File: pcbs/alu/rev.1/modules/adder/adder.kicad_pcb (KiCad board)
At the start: 2 copper layers, 76.2 x 80.6 mm, 513 parts, among them J1 Conn_01x01, J10 Conn_01x01, J11 Conn_01x01, J12 Conn_01x01, J13 Conn_01x01, J14 Conn_01x01, J15 Conn_01x01, J16 Conn_01x01, J17 Conn_01x01, J18 Conn_01x01, J19 Conn_01x01, J2 Conn_01x01, J20 Conn_01x01, J21 Conn_01x01, J22 Conn_01x01, J23 Conn_01x01, J24 Conn_01x01, J25 Conn_01x01, J26 Conn_01x01, J27 Conn_01x01, J28 Conn_01x01, J29 Conn_01x01, J3 Conn_01x01, J30 Conn_01x01, J31 Conn_01x01, J32 Conn_01x01, J33 Conn_01x01, J34 Conn_01x01, J35 Conn_01x01, J36 Conn_01x01, J4 Conn_01x01, J5 Conn_01x01, J6 Conn_01x01, J7 Conn_01x01, J8 Conn_01x01, J9 Conn_01x01, Q1 BSS8402DW, Q10 BSS8402DW, Q100 BSS8402DW, Q101 BSS8402DW, Q102 BSS8402DW, Q103 BSS8402DW, Q104 BSS8402DW, Q105 BSS8402DW, Q106 BSS8402DW, Q107 BSS8402DW, Q108 BSS8402DW, Q109 BSS8402DW, Q11 BSS8402DW, Q110 BSS8402DW, Q111 BSS8402DW, Q112 BSS8402DW, Q113 BSS8402DW, Q114 BSS8402DW, Q115 BSS8402DW, Q116 BSS8402DW, Q117 BSS8402DW, Q118 BSS8402DW, Q119 BSS8402DW, Q12 BSS8402DW, Q120 BSS8402DW, Q121 BSS8402DW, Q122 BSS8402DW, Q123 BSS8402DW, Q124 BSS8402DW, Q125 BSS8402DW, Q126 BSS8402DW, Q127 BSS8402DW, Q128 BSS8402DW, Q129 BSS8402DW, Q13 BSS8402DW, Q130 BSS8402DW, Q131 BSS8402DW, Q132 BSS8402DW, Q133 BSS8402DW, Q134 BSS8402DW, Q135 BSS8402DW, Q136 BSS8402DW, Q137 BSS8402DW, Q138 BSS8402DW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

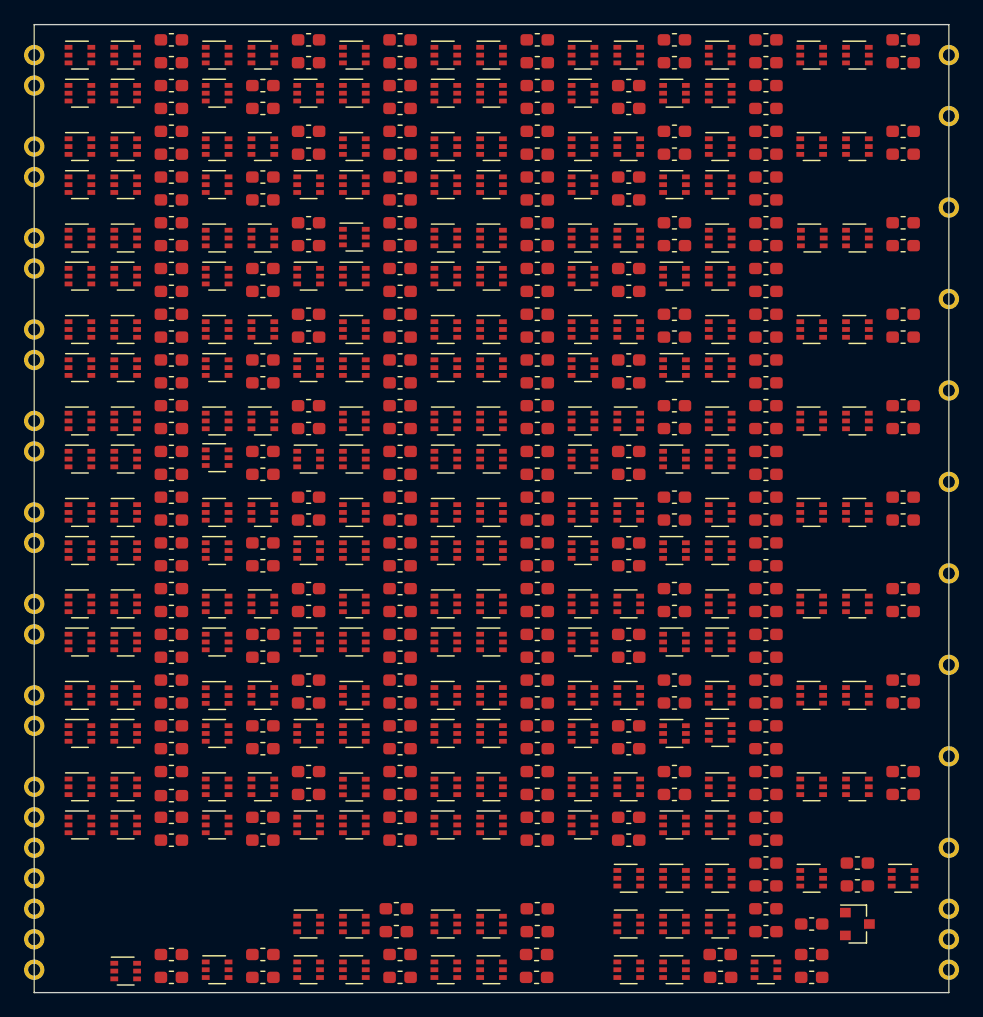
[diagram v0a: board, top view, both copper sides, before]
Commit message: completed adder module for alu
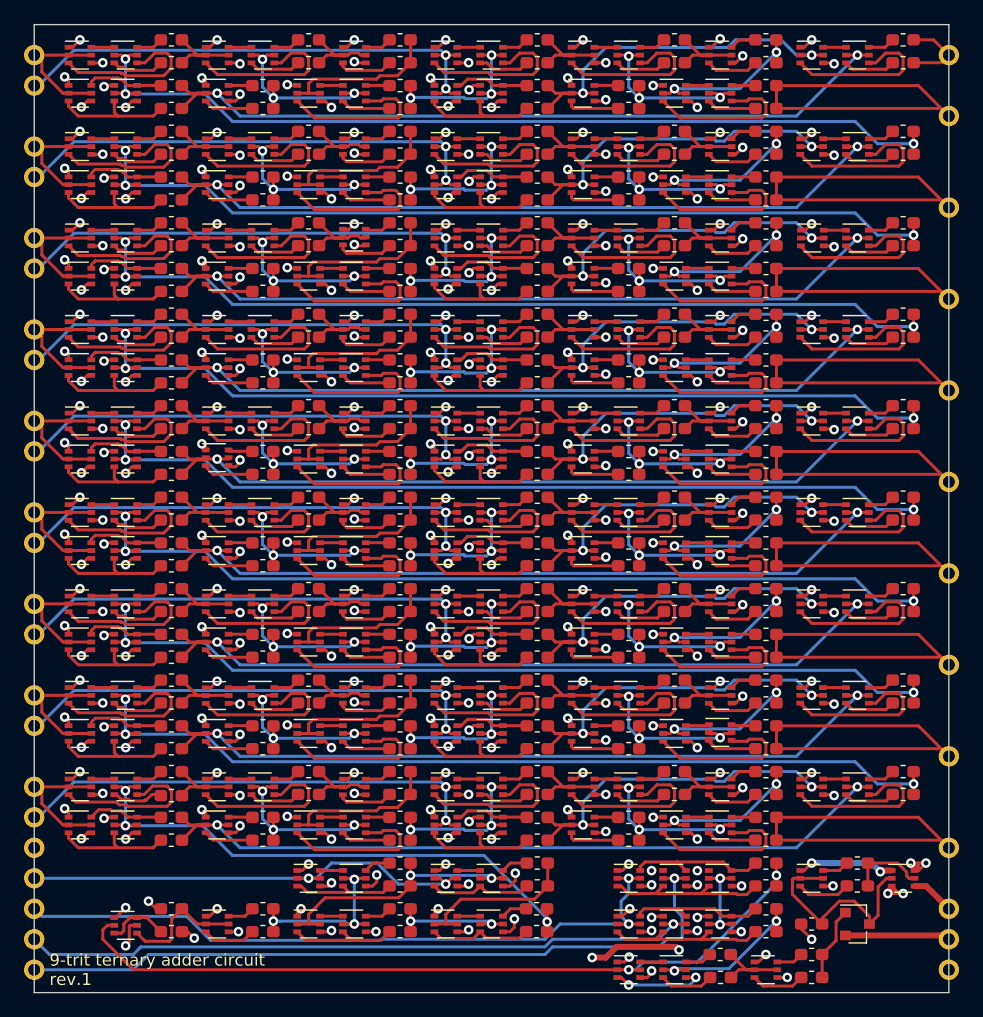
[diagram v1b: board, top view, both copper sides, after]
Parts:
- moved R10 3.82 mm to (182.2, 94.6)
- moved R9 3.82 mm to (182.2, 96.5), turned to 180 degrees
- moved Q14 3.81 mm to (174.6, 99.7)
- moved Q17 3.81 mm to (178.4, 99.7)
- moved Q19 3.81 mm to (186.1, 99.7)
- moved Q20 3.81 mm to (189.9, 99.7)
- moved Q4 3.81 mm to (167.0, 99.7)
- moved R1 3.81 mm to (163.2, 100.3)
- moved R15 3.81 mm to (193.7, 96.5)
- moved R16 3.81 mm to (193.7, 94.6)
- moved R17 3.81 mm to (182.2, 100.3)
- moved R18 3.81 mm to (182.2, 98.4)
- moved R2 3.81 mm to (163.2, 98.4)
- moved R20 3.81 mm to (193.6, 100.3), turned to 180 degrees
- moved R21 3.81 mm to (193.6, 98.4)
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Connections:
- Q1 pad 6: Net-(Q1-Pad4) -> Net-(Q1-Pad3)
- Q10 pad 3: Vdd -> Net-(Q10-Pad3)
- Q10 pad 4: Net-(Q10-Pad4) -> Vdd
- Q101 pad 3: /adder/Vdd -> Net-(Q101-Pad3)
- Q101 pad 4: Net-(Q101-Pad4) -> /adder/Vdd
- Q102 pad 3: /adder/Vdd -> Net-(Q102-Pad3)
- Q102 pad 4: Net-(Q102-Pad4) -> /adder/Vdd
- Q103 pad 3: /adder/Vdd -> Net-(Q103-Pad3)
- Q103 pad 4: Net-(Q103-Pad4) -> /adder/Vdd
- Q104 pad 3: /adder/Vdd -> Net-(Q104-Pad3)
- Q104 pad 4: Net-(Q104-Pad4) -> /adder/Vdd
- Q105 pad 3: /adder/Vdd -> Net-(Q105-Pad3)
- Q105 pad 4: Net-(Q105-Pad4) -> /adder/Vdd
- Q106 pad 3: /adder/Vdd -> Net-(Q106-Pad3)
- Q106 pad 4: Net-(Q106-Pad4) -> /adder/Vdd
- Q107 pad 3: Net-(Q104-Pad4) -> Net-(Q107-Pad3)
- Q107 pad 4: Net-(Q107-Pad4) -> Net-(Q104-Pad3)
- Q108 pad 3: Net-(Q105-Pad4) -> Net-(Q108-Pad3)
- Q108 pad 4: Net-(Q108-Pad4) -> Net-(Q105-Pad3)
- Q109 pad 3: Net-(Q106-Pad4) -> Net-(Q109-Pad3)
- Q109 pad 4: Net-(Q109-Pad4) -> Net-(Q106-Pad3)
- Q11 pad 3: Vdd -> Net-(Q11-Pad3)
- Q11 pad 4: Net-(Q11-Pad4) -> Vdd
- Q110 pad 3: /adder/Vdd -> Net-(Q110-Pad3)
- Q110 pad 4: Net-(Q110-Pad4) -> /adder/Vdd
- Q111 pad 3: /adder/Vdd -> Net-(Q111-Pad3)
- Q111 pad 4: Net-(Q111-Pad4) -> /adder/Vdd
- Q112 pad 3: /adder/Vdd -> Net-(Q112-Pad3)
- Q112 pad 4: Net-(Q112-Pad4) -> /adder/Vdd
- Q113 pad 3: /adder/Vdd -> Net-(Q113-Pad3)
- Q113 pad 4: Net-(Q113-Pad4) -> /adder/Vdd
- Q114 pad 3: /adder/Vdd -> Net-(Q114-Pad3)
- Q114 pad 4: Net-(Q114-Pad4) -> /adder/Vdd
- Q115 pad 3: /adder/Vdd -> Net-(Q115-Pad3)
- Q115 pad 4: Net-(Q115-Pad4) -> /adder/Vdd
- Q116 pad 3: Net-(Q113-Pad4) -> Net-(Q116-Pad3)
- Q116 pad 4: Net-(Q116-Pad4) -> Net-(Q113-Pad3)
- Q117 pad 3: Net-(Q114-Pad4) -> Net-(Q117-Pad3)
- Q117 pad 4: Net-(Q117-Pad4) -> Net-(Q114-Pad3)
- Q118 pad 3: Net-(Q115-Pad4) -> Net-(Q118-Pad3)
- Q118 pad 4: Net-(Q118-Pad4) -> Net-(Q115-Pad3)
- Q119 pad 3: /adder/Vdd -> Net-(Q119-Pad3)
- Q119 pad 4: Net-(Q119-Pad4) -> /adder/Vdd
- Q12 pad 3: Net-(Q11-Pad4) -> Net-(Q12-Pad3)
- Q12 pad 4: Net-(Q12-Pad4) -> Net-(Q11-Pad3)
- Q120 pad 3: /adder/Vdd -> Net-(Q120-Pad3)
- Q120 pad 4: Net-(Q120-Pad4) -> /adder/Vdd
- Q121 pad 3: /adder/Vdd -> Net-(Q121-Pad3)
- Q121 pad 4: Net-(Q121-Pad4) -> /adder/Vdd
- Q122 pad 3: /adder/Vdd -> Net-(Q122-Pad3)
- Q122 pad 4: Net-(Q122-Pad4) -> /adder/Vdd
- Q123 pad 3: /adder/Vdd -> Net-(Q123-Pad3)
- Q123 pad 4: Net-(Q123-Pad4) -> /adder/Vdd
- Q124 pad 3: /adder/Vdd -> Net-(Q124-Pad3)
- Q124 pad 4: Net-(Q124-Pad4) -> /adder/Vdd
- Q125 pad 3: /adder/Vdd -> Net-(Q120-Pad3)
- Q125 pad 4: Net-(Q120-Pad4) -> /adder/Vdd
- Q126 pad 3: /adder/Vdd -> Net-(Q122-Pad3)
- Q126 pad 4: Net-(Q122-Pad4) -> /adder/Vdd
- Q127 pad 3: /adder/Vdd -> Net-(Q124-Pad3)
- Q127 pad 4: Net-(Q124-Pad4) -> /adder/Vdd
- Q128 pad 3: Net-(Q119-Pad4) -> Net-(Q128-Pad3)
- Q128 pad 4: Net-(Q128-Pad4) -> Net-(Q119-Pad3)
- Q129 pad 3: Net-(Q121-Pad4) -> Net-(Q129-Pad3)
- Q129 pad 4: Net-(Q129-Pad4) -> Net-(Q121-Pad3)
- Q13 pad 3: Vdd -> Net-(Q13-Pad3)
- Q13 pad 4: Net-(Q13-Pad4) -> Vdd
- Q130 pad 3: Net-(Q123-Pad4) -> Net-(Q130-Pad3)
- Q130 pad 4: Net-(Q130-Pad4) -> Net-(Q123-Pad3)
- Q131 pad 3: /adder/Vdd -> Net-(Q131-Pad3)
- Q131 pad 4: Net-(Q131-Pad4) -> /adder/Vdd
- Q132 pad 3: /adder/Vdd -> Net-(Q132-Pad3)
- Q132 pad 4: Net-(Q132-Pad4) -> /adder/Vdd
- Q133 pad 3: /adder/Vdd -> Net-(Q133-Pad3)
- Q133 pad 4: Net-(Q133-Pad4) -> /adder/Vdd
- Q134 pad 3: /adder/Vdd -> Net-(Q134-Pad3)
- Q134 pad 4: Net-(Q134-Pad4) -> /adder/Vdd
- Q135 pad 3: /adder/Vdd -> Net-(Q135-Pad3)
- Q135 pad 4: Net-(Q135-Pad4) -> /adder/Vdd
- Q136 pad 3: /adder/Vdd -> Net-(Q136-Pad3)
- Q136 pad 4: Net-(Q136-Pad4) -> /adder/Vdd
- Q137 pad 3: Net-(Q134-Pad4) -> Net-(Q137-Pad3)
- Q137 pad 4: Net-(Q137-Pad4) -> Net-(Q134-Pad3)
- Q138 pad 3: Net-(Q135-Pad4) -> Net-(Q138-Pad3)
- Q138 pad 4: Net-(Q138-Pad4) -> Net-(Q135-Pad3)
- Q139 pad 3: Net-(Q136-Pad4) -> Net-(Q139-Pad3)
- Q139 pad 4: Net-(Q139-Pad4) -> Net-(Q136-Pad3)
- Q14 pad 3: Vdd -> Net-(Q14-Pad3)
- Q14 pad 4: Net-(Q14-Pad4) -> Vdd
- Q140 pad 3: /adder/Vdd -> Net-(Q140-Pad3)
- Q140 pad 4: Net-(Q140-Pad4) -> /adder/Vdd
- Q141 pad 3: /adder/Vdd -> Net-(Q141-Pad3)
- Q141 pad 4: Net-(Q141-Pad4) -> /adder/Vdd
- Q142 pad 3: /adder/Vdd -> Net-(Q142-Pad3)
- Q142 pad 4: Net-(Q142-Pad4) -> /adder/Vdd
- Q143 pad 3: /adder/Vdd -> Net-(Q143-Pad3)
- Q143 pad 4: Net-(Q143-Pad4) -> /adder/Vdd
- Q144 pad 3: /adder/Vdd -> Net-(Q144-Pad3)
- Q144 pad 4: Net-(Q144-Pad4) -> /adder/Vdd
- Q145 pad 3: /adder/Vdd -> Net-(Q145-Pad3)
- Q145 pad 4: Net-(Q145-Pad4) -> /adder/Vdd
- Q146 pad 3: Net-(Q143-Pad4) -> Net-(Q146-Pad3)
- Q146 pad 4: Net-(Q146-Pad4) -> Net-(Q143-Pad3)
- Q147 pad 3: Net-(Q144-Pad4) -> Net-(Q147-Pad3)
- Q147 pad 4: Net-(Q147-Pad4) -> Net-(Q144-Pad3)
- Q148 pad 3: Net-(Q145-Pad4) -> Net-(Q148-Pad3)
- Q148 pad 4: Net-(Q148-Pad4) -> Net-(Q145-Pad3)
- Q149 pad 3: /adder/Vdd -> Net-(Q149-Pad3)
- Q149 pad 4: Net-(Q149-Pad4) -> /adder/Vdd
- Q15 pad 3: Vdd -> Net-(Q15-Pad3)
- Q15 pad 4: Net-(Q15-Pad4) -> Vdd
- Q150 pad 3: /adder/Vdd -> Net-(Q150-Pad3)
- Q150 pad 4: Net-(Q150-Pad4) -> /adder/Vdd
- Q151 pad 3: /adder/Vdd -> Net-(Q151-Pad3)
- Q151 pad 4: Net-(Q151-Pad4) -> /adder/Vdd
- Q152 pad 3: Net-(Q149-Pad4) -> Net-(Q152-Pad3)
- Q152 pad 4: Net-(Q152-Pad4) -> Net-(Q149-Pad3)
- Q153 pad 3: Net-(Q150-Pad4) -> Net-(Q153-Pad3)
- Q153 pad 4: Net-(Q153-Pad4) -> Net-(Q150-Pad3)
- Q154 pad 3: Net-(Q151-Pad4) -> Net-(Q154-Pad3)
- Q154 pad 4: Net-(Q154-Pad4) -> Net-(Q151-Pad3)
- Q155 pad 3: /adder/Vdd -> Net-(Q155-Pad3)
- Q155 pad 4: Net-(Q155-Pad4) -> /adder/Vdd
- Q156 pad 3: /adder/Vdd -> Net-(Q156-Pad3)
- Q156 pad 4: Net-(Q156-Pad4) -> /adder/Vdd
- Q157 pad 3: /adder/Vdd -> Net-(Q157-Pad3)
- Q157 pad 4: Net-(Q157-Pad4) -> /adder/Vdd
- Q158 pad 3: /adder/Vdd -> Net-(Q158-Pad3)
- Q158 pad 4: Net-(Q158-Pad4) -> /adder/Vdd
- Q159 pad 3: /adder/Vdd -> Net-(Q159-Pad3)
- Q159 pad 4: Net-(Q159-Pad4) -> /adder/Vdd
- Q16 pad 3: Vdd -> Net-(Q13-Pad3)
- Q16 pad 4: Net-(Q13-Pad4) -> Vdd
- Q160 pad 3: /adder/Vdd -> Net-(Q160-Pad3)
- Q160 pad 4: Net-(Q160-Pad4) -> /adder/Vdd
- Q161 pad 3: /adder/Vdd -> Net-(Q156-Pad3)
- Q161 pad 4: Net-(Q156-Pad4) -> /adder/Vdd
- Q162 pad 3: /adder/Vdd -> Net-(Q158-Pad3)
- Q162 pad 4: Net-(Q158-Pad4) -> /adder/Vdd
- Q163 pad 3: /adder/Vdd -> Net-(Q160-Pad3)
- Q163 pad 4: Net-(Q160-Pad4) -> /adder/Vdd
- Q164 pad 3: Net-(Q155-Pad4) -> Net-(Q164-Pad3)
- Q164 pad 4: Net-(Q164-Pad4) -> Net-(Q155-Pad3)
- Q165 pad 3: Net-(Q157-Pad4) -> Net-(Q165-Pad3)
- Q165 pad 4: Net-(Q165-Pad4) -> Net-(Q157-Pad3)
- Q166 pad 3: Net-(Q159-Pad4) -> Net-(Q166-Pad3)
- Q166 pad 4: Net-(Q166-Pad4) -> Net-(Q159-Pad3)
- Q167 pad 3: /adder/Vdd -> Net-(Q167-Pad3)
- Q167 pad 4: Net-(Q167-Pad4) -> /adder/Vdd
- Q168 pad 3: /adder/Vdd -> Net-(Q168-Pad3)
- Q168 pad 4: Net-(Q168-Pad4) -> /adder/Vdd
- Q169 pad 3: /adder/Vdd -> Net-(Q169-Pad3)
- Q169 pad 4: Net-(Q169-Pad4) -> /adder/Vdd
- Q17 pad 3: Vdd -> Net-(Q14-Pad3)
- Q17 pad 4: Net-(Q14-Pad4) -> Vdd
- Q170 pad 3: /adder/Vdd -> Net-(Q170-Pad3)
- Q170 pad 4: Net-(Q170-Pad4) -> /adder/Vdd
- Q171 pad 3: /adder/Vdd -> Net-(Q171-Pad3)
- Q171 pad 4: Net-(Q171-Pad4) -> /adder/Vdd
- Q172 pad 3: /adder/Vdd -> Net-(Q172-Pad3)
- Q172 pad 4: Net-(Q172-Pad4) -> /adder/Vdd
- Q173 pad 3: Net-(Q170-Pad4) -> Net-(Q173-Pad3)
- Q173 pad 4: Net-(Q173-Pad4) -> Net-(Q170-Pad3)
- Q174 pad 3: Net-(Q171-Pad4) -> Net-(Q174-Pad3)
- Q174 pad 4: Net-(Q174-Pad4) -> Net-(Q171-Pad3)
- Q175 pad 3: Net-(Q172-Pad4) -> Net-(Q175-Pad3)
- Q175 pad 4: Net-(Q175-Pad4) -> Net-(Q172-Pad3)
- Q176 pad 3: /adder/Vdd -> Net-(Q176-Pad3)
- Q176 pad 4: Net-(Q176-Pad4) -> /adder/Vdd
- Q177 pad 3: /adder/Vdd -> Net-(Q177-Pad3)
- Q177 pad 4: Net-(Q177-Pad4) -> /adder/Vdd
- Q178 pad 3: /adder/Vdd -> Net-(Q178-Pad3)
- Q178 pad 4: Net-(Q178-Pad4) -> /adder/Vdd
- Q179 pad 3: /adder/Vdd -> Net-(Q179-Pad3)
- Q179 pad 4: Net-(Q179-Pad4) -> /adder/Vdd
- Q180 pad 3: /adder/Vdd -> Net-(Q180-Pad3)
- Q180 pad 4: Net-(Q180-Pad4) -> /adder/Vdd
- Q181 pad 3: /adder/Vdd -> Net-(Q181-Pad3)
- Q181 pad 4: Net-(Q181-Pad4) -> /adder/Vdd
- Q182 pad 3: Net-(Q179-Pad4) -> Net-(Q182-Pad3)
- Q182 pad 4: Net-(Q182-Pad4) -> Net-(Q179-Pad3)
- Q183 pad 3: Net-(Q180-Pad4) -> Net-(Q183-Pad3)
- Q183 pad 4: Net-(Q183-Pad4) -> Net-(Q180-Pad3)
- Q184 pad 3: Net-(Q181-Pad4) -> Net-(Q184-Pad3)
- Q184 pad 4: Net-(Q184-Pad4) -> Net-(Q181-Pad3)
- Q185 pad 3: /adder/Vdd -> Net-(Q185-Pad3)
- Q185 pad 4: Net-(Q185-Pad4) -> /adder/Vdd
- Q186 pad 3: /adder/Vdd -> Net-(Q186-Pad3)
- Q186 pad 4: Net-(Q186-Pad4) -> /adder/Vdd
- Q187 pad 3: /adder/Vdd -> Net-(Q187-Pad3)
- Q187 pad 4: Net-(Q187-Pad4) -> /adder/Vdd
- Q188 pad 3: /adder/Vdd -> Net-(Q188-Pad3)
- Q188 pad 4: Net-(Q188-Pad4) -> /adder/Vdd
- Q189 pad 3: /adder/Vdd -> Net-(Q189-Pad3)
- Q189 pad 4: Net-(Q189-Pad4) -> /adder/Vdd
- Q19 pad 3: Vdd -> Net-(Q19-Pad3)
- Q19 pad 4: Net-(Q19-Pad4) -> Vdd
- Q190 pad 3: /adder/Vdd -> Net-(Q190-Pad3)
- Q190 pad 4: Net-(Q190-Pad4) -> /adder/Vdd
- Q191 pad 3: /adder/Vdd -> Net-(Q186-Pad3)
- Q191 pad 4: Net-(Q186-Pad4) -> /adder/Vdd
- Q192 pad 3: /adder/Vdd -> Net-(Q188-Pad3)
- Q192 pad 4: Net-(Q188-Pad4) -> /adder/Vdd
- Q193 pad 3: /adder/Vdd -> Net-(Q190-Pad3)
- Q193 pad 4: Net-(Q190-Pad4) -> /adder/Vdd
- Q194 pad 3: Net-(Q185-Pad4) -> Net-(Q194-Pad3)
- Q194 pad 4: Net-(Q194-Pad4) -> Net-(Q185-Pad3)
- Q195 pad 3: Net-(Q187-Pad4) -> Net-(Q195-Pad3)
- Q195 pad 4: Net-(Q195-Pad4) -> Net-(Q187-Pad3)
- Q196 pad 3: Net-(Q189-Pad4) -> Net-(Q196-Pad3)
- Q196 pad 4: Net-(Q196-Pad4) -> Net-(Q189-Pad3)
- Q197 pad 3: /adder/Vdd -> Net-(Q197-Pad3)
- Q197 pad 4: Net-(Q197-Pad4) -> /adder/Vdd
- Q198 pad 3: /adder/Vdd -> Net-(Q198-Pad3)
- Q198 pad 4: Net-(Q198-Pad4) -> /adder/Vdd
- Q199 pad 3: /adder/Vdd -> Net-(Q199-Pad3)
- Q199 pad 4: Net-(Q199-Pad4) -> /adder/Vdd
- Q2 pad 3: Vdd -> Net-(Q2-Pad3)
- Q2 pad 4: Net-(Q2-Pad4) -> Vdd
- Q20 pad 3: Vdd -> Net-(Q19-Pad3)
- Q20 pad 4: Net-(Q19-Pad4) -> Vdd
- Q200 pad 3: /adder/Vdd -> Net-(Q200-Pad3)
- Q200 pad 4: Net-(Q200-Pad4) -> /adder/Vdd
- Q201 pad 3: /adder/Vdd -> Net-(Q201-Pad3)
- Q201 pad 4: Net-(Q201-Pad4) -> /adder/Vdd
- Q202 pad 3: /adder/Vdd -> Net-(Q202-Pad3)
- Q202 pad 4: Net-(Q202-Pad4) -> /adder/Vdd
- Q203 pad 3: Net-(Q200-Pad4) -> Net-(Q203-Pad3)
- Q203 pad 4: Net-(Q203-Pad4) -> Net-(Q200-Pad3)
- Q204 pad 3: Net-(Q201-Pad4) -> Net-(Q204-Pad3)
- Q204 pad 4: Net-(Q204-Pad4) -> Net-(Q201-Pad3)
- Q205 pad 3: Net-(Q202-Pad4) -> Net-(Q205-Pad3)
- Q205 pad 4: Net-(Q205-Pad4) -> Net-(Q202-Pad3)
- Q206 pad 3: /adder/Vdd -> Net-(Q206-Pad3)
- Q206 pad 4: Net-(Q206-Pad4) -> /adder/Vdd
- Q207 pad 3: /adder/Vdd -> Net-(Q207-Pad3)
- Q207 pad 4: Net-(Q207-Pad4) -> /adder/Vdd
- Q208 pad 3: /adder/Vdd -> Net-(Q208-Pad3)
- Q208 pad 4: Net-(Q208-Pad4) -> /adder/Vdd
- Q209 pad 3: /adder/Vdd -> Net-(Q209-Pad3)
- Q209 pad 4: Net-(Q209-Pad4) -> /adder/Vdd
- Q21 pad 3: Vdd -> Net-(Q21-Pad3)
- Q21 pad 4: Net-(Q21-Pad4) -> Vdd
- Q210 pad 3: /adder/Vdd -> Net-(Q210-Pad3)
- Q210 pad 4: Net-(Q210-Pad4) -> /adder/Vdd
- Q211 pad 3: /adder/Vdd -> Net-(Q211-Pad3)
- Q211 pad 4: Net-(Q211-Pad4) -> /adder/Vdd
- Q212 pad 3: Net-(Q209-Pad4) -> Net-(Q212-Pad3)
- Q212 pad 4: Net-(Q212-Pad4) -> Net-(Q209-Pad3)
- Q213 pad 3: Net-(Q210-Pad4) -> Net-(Q213-Pad3)
- Q213 pad 4: Net-(Q213-Pad4) -> Net-(Q210-Pad3)
- Q214 pad 3: Net-(Q211-Pad4) -> Net-(Q214-Pad3)
- Q214 pad 4: Net-(Q214-Pad4) -> Net-(Q211-Pad3)
- Q215 pad 3: /adder/Vdd -> Net-(Q215-Pad3)
- Q215 pad 4: Net-(Q215-Pad4) -> /adder/Vdd
- Q216 pad 3: /adder/Vdd -> Net-(Q216-Pad3)
- Q216 pad 4: Net-(Q216-Pad4) -> /adder/Vdd
- Q217 pad 3: /adder/Vdd -> Net-(Q217-Pad3)
- Q217 pad 4: Net-(Q217-Pad4) -> /adder/Vdd
- Q218 pad 3: Net-(Q215-Pad4) -> Net-(Q218-Pad3)
- Q218 pad 4: Net-(Q218-Pad4) -> Net-(Q215-Pad3)
- Q219 pad 3: Net-(Q216-Pad4) -> Net-(Q219-Pad3)
- Q219 pad 4: Net-(Q219-Pad4) -> Net-(Q216-Pad3)
- Q22 pad 3: Vdd -> /adder/Vdd
- Q22 pad 4: /adder/Vdd -> Vdd
- Q220 pad 3: Net-(Q217-Pad4) -> Net-(Q220-Pad3)
- Q220 pad 4: Net-(Q220-Pad4) -> Net-(Q217-Pad3)
- Q23 pad 3: /adder/Vdd -> Net-(Q23-Pad3)
- Q23 pad 4: Net-(Q23-Pad4) -> /adder/Vdd
- Q24 pad 3: /adder/Vdd -> Net-(Q24-Pad3)
- Q24 pad 4: Net-(Q24-Pad4) -> /adder/Vdd
- Q25 pad 3: /adder/Vdd -> Net-(Q25-Pad3)
- Q25 pad 4: Net-(Q25-Pad4) -> /adder/Vdd
- Q26 pad 3: /adder/Vdd -> Net-(Q26-Pad3)
- Q26 pad 4: Net-(Q26-Pad4) -> /adder/Vdd
- Q27 pad 3: /adder/Vdd -> Net-(Q27-Pad3)
- Q27 pad 4: Net-(Q27-Pad4) -> /adder/Vdd
- Q28 pad 3: /adder/Vdd -> Net-(Q28-Pad3)
- Q28 pad 4: Net-(Q28-Pad4) -> /adder/Vdd
- Q29 pad 3: /adder/Vdd -> Net-(Q24-Pad3)
- Q29 pad 4: Net-(Q24-Pad4) -> /adder/Vdd
- Q3 pad 3: Vdd -> Net-(Q3-Pad3)
- Q3 pad 4: Net-(Q3-Pad4) -> Vdd
- Q30 pad 3: /adder/Vdd -> Net-(Q26-Pad3)
- Q30 pad 4: Net-(Q26-Pad4) -> /adder/Vdd
- Q31 pad 3: /adder/Vdd -> Net-(Q28-Pad3)
- Q31 pad 4: Net-(Q28-Pad4) -> /adder/Vdd
- Q32 pad 3: Net-(Q23-Pad4) -> Net-(Q32-Pad3)
- Q32 pad 4: Net-(Q32-Pad4) -> Net-(Q23-Pad3)
- Q33 pad 3: Net-(Q25-Pad4) -> Net-(Q33-Pad3)
- Q33 pad 4: Net-(Q33-Pad4) -> Net-(Q25-Pad3)
- Q34 pad 3: Net-(Q27-Pad4) -> Net-(Q34-Pad3)
- Q34 pad 4: Net-(Q34-Pad4) -> Net-(Q27-Pad3)
- Q35 pad 3: /adder/Vdd -> Net-(Q35-Pad3)
- Q35 pad 4: Net-(Q35-Pad4) -> /adder/Vdd
- Q36 pad 3: /adder/Vdd -> Net-(Q36-Pad3)
- Q36 pad 4: Net-(Q36-Pad4) -> /adder/Vdd
- Q37 pad 3: /adder/Vdd -> Net-(Q37-Pad3)
- Q37 pad 4: Net-(Q37-Pad4) -> /adder/Vdd
- Q38 pad 3: /adder/Vdd -> Net-(Q38-Pad3)
- Q38 pad 4: Net-(Q38-Pad4) -> /adder/Vdd
- Q39 pad 3: /adder/Vdd -> Net-(Q39-Pad3)
- Q39 pad 4: Net-(Q39-Pad4) -> /adder/Vdd
- Q4 pad 2: Net-(Q1-Pad3) -> Net-(Q1-Pad4)
- Q4 pad 3: Vdd -> Net-(Q4-Pad3)
- Q4 pad 4: Net-(Q4-Pad4) -> Vdd
- Q4 pad 5: Net-(Q1-Pad3) -> Net-(Q1-Pad4)
- Q40 pad 3: /adder/Vdd -> Net-(Q40-Pad3)
- Q40 pad 4: Net-(Q40-Pad4) -> /adder/Vdd
- Q41 pad 3: Net-(Q38-Pad4) -> Net-(Q41-Pad3)
- Q41 pad 4: Net-(Q41-Pad4) -> Net-(Q38-Pad3)
- Q42 pad 3: Net-(Q39-Pad4) -> Net-(Q42-Pad3)
- Q42 pad 4: Net-(Q42-Pad4) -> Net-(Q39-Pad3)
- Q43 pad 3: Net-(Q40-Pad4) -> Net-(Q43-Pad3)
- Q43 pad 4: Net-(Q43-Pad4) -> Net-(Q40-Pad3)
- Q44 pad 3: /adder/Vdd -> Net-(Q44-Pad3)
- Q44 pad 4: Net-(Q44-Pad4) -> /adder/Vdd
- Q45 pad 3: /adder/Vdd -> Net-(Q45-Pad3)
- Q45 pad 4: Net-(Q45-Pad4) -> /adder/Vdd
- Q46 pad 3: /adder/Vdd -> Net-(Q46-Pad3)
- Q46 pad 4: Net-(Q46-Pad4) -> /adder/Vdd
- Q47 pad 3: /adder/Vdd -> Net-(Q47-Pad3)
- Q47 pad 4: Net-(Q47-Pad4) -> /adder/Vdd
- Q48 pad 3: /adder/Vdd -> Net-(Q48-Pad3)
- Q48 pad 4: Net-(Q48-Pad4) -> /adder/Vdd
- Q49 pad 3: /adder/Vdd -> Net-(Q49-Pad3)
- Q49 pad 4: Net-(Q49-Pad4) -> /adder/Vdd
- Q5 pad 3: Vdd -> Net-(Q2-Pad3)
- Q5 pad 4: Net-(Q2-Pad4) -> Vdd
- Q50 pad 3: Net-(Q47-Pad4) -> Net-(Q50-Pad3)
- Q50 pad 4: Net-(Q50-Pad4) -> Net-(Q47-Pad3)
- Q51 pad 3: Net-(Q48-Pad4) -> Net-(Q51-Pad3)
- Q51 pad 4: Net-(Q51-Pad4) -> Net-(Q48-Pad3)
- Q52 pad 3: Net-(Q49-Pad4) -> Net-(Q52-Pad3)
- Q52 pad 4: Net-(Q52-Pad4) -> Net-(Q49-Pad3)
- Q53 pad 3: /adder/Vdd -> Net-(Q53-Pad3)
- Q53 pad 4: Net-(Q53-Pad4) -> /adder/Vdd
- Q54 pad 3: /adder/Vdd -> Net-(Q54-Pad3)
- Q54 pad 4: Net-(Q54-Pad4) -> /adder/Vdd
- Q55 pad 3: /adder/Vdd -> Net-(Q55-Pad3)
- Q55 pad 4: Net-(Q55-Pad4) -> /adder/Vdd
- Q56 pad 3: /adder/Vdd -> Net-(Q56-Pad3)
- Q56 pad 4: Net-(Q56-Pad4) -> /adder/Vdd
- Q57 pad 3: /adder/Vdd -> Net-(Q57-Pad3)
- Q57 pad 4: Net-(Q57-Pad4) -> /adder/Vdd
- Q58 pad 3: /adder/Vdd -> Net-(Q58-Pad3)
- Q58 pad 4: Net-(Q58-Pad4) -> /adder/Vdd
- Q59 pad 3: /adder/Vdd -> Net-(Q54-Pad3)
- Q59 pad 4: Net-(Q54-Pad4) -> /adder/Vdd
- Q6 pad 3: Vdd -> Net-(Q3-Pad3)
- Q6 pad 4: Net-(Q3-Pad4) -> Vdd
- Q60 pad 3: /adder/Vdd -> Net-(Q56-Pad3)
- Q60 pad 4: Net-(Q56-Pad4) -> /adder/Vdd
- Q61 pad 3: /adder/Vdd -> Net-(Q58-Pad3)
- Q61 pad 4: Net-(Q58-Pad4) -> /adder/Vdd
- Q62 pad 3: Net-(Q53-Pad4) -> Net-(Q62-Pad3)
- Q62 pad 4: Net-(Q62-Pad4) -> Net-(Q53-Pad3)
- Q63 pad 3: Net-(Q55-Pad4) -> Net-(Q63-Pad3)
- Q63 pad 4: Net-(Q63-Pad4) -> Net-(Q55-Pad3)
- Q64 pad 3: Net-(Q57-Pad4) -> Net-(Q64-Pad3)
- Q64 pad 4: Net-(Q64-Pad4) -> Net-(Q57-Pad3)
- Q65 pad 3: /adder/Vdd -> Net-(Q65-Pad3)
- Q65 pad 4: Net-(Q65-Pad4) -> /adder/Vdd
- Q66 pad 3: /adder/Vdd -> Net-(Q66-Pad3)
- Q66 pad 4: Net-(Q66-Pad4) -> /adder/Vdd
- Q67 pad 3: /adder/Vdd -> Net-(Q67-Pad3)
- Q67 pad 4: Net-(Q67-Pad4) -> /adder/Vdd
- Q68 pad 3: /adder/Vdd -> Net-(Q68-Pad3)
- Q68 pad 4: Net-(Q68-Pad4) -> /adder/Vdd
- Q69 pad 3: /adder/Vdd -> Net-(Q69-Pad3)
- Q69 pad 4: Net-(Q69-Pad4) -> /adder/Vdd
- Q7 pad 3: Vdd -> Net-(Q2-Pad3)
- Q7 pad 4: Net-(Q2-Pad4) -> Vdd
- Q70 pad 3: /adder/Vdd -> Net-(Q70-Pad3)
- Q70 pad 4: Net-(Q70-Pad4) -> /adder/Vdd
- Q71 pad 3: Net-(Q68-Pad4) -> Net-(Q71-Pad3)
- Q71 pad 4: Net-(Q71-Pad4) -> Net-(Q68-Pad3)
- Q72 pad 3: Net-(Q69-Pad4) -> Net-(Q72-Pad3)
- Q72 pad 4: Net-(Q72-Pad4) -> Net-(Q69-Pad3)
- Q73 pad 3: Net-(Q70-Pad4) -> Net-(Q73-Pad3)
- Q73 pad 4: Net-(Q73-Pad4) -> Net-(Q70-Pad3)
- Q74 pad 3: /adder/Vdd -> Net-(Q74-Pad3)
- Q74 pad 4: Net-(Q74-Pad4) -> /adder/Vdd
- Q75 pad 3: /adder/Vdd -> Net-(Q75-Pad3)
- Q75 pad 4: Net-(Q75-Pad4) -> /adder/Vdd
- Q76 pad 3: /adder/Vdd -> Net-(Q76-Pad3)
- Q76 pad 4: Net-(Q76-Pad4) -> /adder/Vdd
- Q77 pad 3: /adder/Vdd -> Net-(Q77-Pad3)
- Q77 pad 4: Net-(Q77-Pad4) -> /adder/Vdd
- Q78 pad 3: /adder/Vdd -> Net-(Q78-Pad3)
- Q78 pad 4: Net-(Q78-Pad4) -> /adder/Vdd
- Q79 pad 3: /adder/Vdd -> Net-(Q79-Pad3)
- Q79 pad 4: Net-(Q79-Pad4) -> /adder/Vdd
- Q8 pad 3: Vdd -> Net-(Q3-Pad3)
- Q8 pad 4: Net-(Q3-Pad4) -> Vdd
- Q80 pad 3: Net-(Q77-Pad4) -> Net-(Q80-Pad3)
- Q80 pad 4: Net-(Q80-Pad4) -> Net-(Q77-Pad3)
- Q81 pad 3: Net-(Q78-Pad4) -> Net-(Q81-Pad3)
- Q81 pad 4: Net-(Q81-Pad4) -> Net-(Q78-Pad3)
- Q82 pad 3: Net-(Q79-Pad4) -> Net-(Q82-Pad3)
- Q82 pad 4: Net-(Q82-Pad4) -> Net-(Q79-Pad3)
- Q83 pad 3: /adder/Vdd -> Net-(Q83-Pad3)
- Q83 pad 4: Net-(Q83-Pad4) -> /adder/Vdd
- Q84 pad 3: /adder/Vdd -> Net-(Q84-Pad3)
- Q84 pad 4: Net-(Q84-Pad4) -> /adder/Vdd
- Q85 pad 3: /adder/Vdd -> Net-(Q85-Pad3)
- Q85 pad 4: Net-(Q85-Pad4) -> /adder/Vdd
- Q86 pad 3: Net-(Q83-Pad4) -> Net-(Q86-Pad3)
- Q86 pad 4: Net-(Q86-Pad4) -> Net-(Q83-Pad3)
- Q87 pad 3: Net-(Q84-Pad4) -> Net-(Q87-Pad3)
- Q87 pad 4: Net-(Q87-Pad4) -> Net-(Q84-Pad3)
- Q88 pad 3: Net-(Q85-Pad4) -> Net-(Q88-Pad3)
- Q88 pad 4: Net-(Q88-Pad4) -> Net-(Q85-Pad3)
- Q89 pad 3: /adder/Vdd -> Net-(Q89-Pad3)
- Q89 pad 4: Net-(Q89-Pad4) -> /adder/Vdd
- Q9 pad 3: Vdd -> Net-(Q10-Pad3)
- Q9 pad 4: Net-(Q10-Pad4) -> Vdd
- Q90 pad 3: /adder/Vdd -> Net-(Q90-Pad3)
- Q90 pad 4: Net-(Q90-Pad4) -> /adder/Vdd
- Q91 pad 3: /adder/Vdd -> Net-(Q91-Pad3)
- Q91 pad 4: Net-(Q91-Pad4) -> /adder/Vdd
- Q92 pad 3: /adder/Vdd -> Net-(Q92-Pad3)
- Q92 pad 4: Net-(Q92-Pad4) -> /adder/Vdd
- Q93 pad 3: /adder/Vdd -> Net-(Q100-Pad4)
- Q93 pad 4: Net-(Q100-Pad3) -> /adder/Vdd
- Q94 pad 3: /adder/Vdd -> Net-(Q94-Pad3)
- Q94 pad 4: Net-(Q94-Pad4) -> /adder/Vdd
- Q95 pad 3: /adder/Vdd -> Net-(Q90-Pad3)
- Q95 pad 4: Net-(Q90-Pad4) -> /adder/Vdd
- Q96 pad 3: /adder/Vdd -> Net-(Q92-Pad3)
- Q96 pad 4: Net-(Q92-Pad4) -> /adder/Vdd
- Q97 pad 3: /adder/Vdd -> Net-(Q94-Pad3)
- Q97 pad 4: Net-(Q94-Pad4) -> /adder/Vdd
- Q98 pad 3: Net-(Q89-Pad4) -> Net-(Q98-Pad3)
- Q98 pad 4: Net-(Q98-Pad4) -> Net-(Q89-Pad3)
- Q99 pad 3: Net-(Q91-Pad4) -> Net-(Q99-Pad3)
- Q99 pad 4: Net-(Q99-Pad4) -> Net-(Q91-Pad3)
- R1 pad 1: Net-(Q1-Pad4) -> Net-(Q1-Pad3)
- R100 pad 2: Net-(Q88-Pad4) -> Net-(Q88-Pad3)
- R102 pad 2: Net-(Q90-Pad4) -> Net-(Q90-Pad3)
- R104 pad 2: Net-(Q92-Pad4) -> Net-(Q92-Pad3)
- R106 pad 2: Net-(Q94-Pad4) -> Net-(Q94-Pad3)
- R108 pad 2: Net-(Q98-Pad4) -> Net-(Q98-Pad3)
- R11 pad 2: Net-(Q12-Pad4) -> Net-(Q12-Pad3)
- R110 pad 2: Net-(Q99-Pad4) -> Net-(Q99-Pad3)
- R112 pad 2: Net-(Q100-Pad4) -> Net-(Q100-Pad3)
- R114 pad 2: Net-(Q101-Pad4) -> Net-(Q101-Pad3)
- R116 pad 2: Net-(Q102-Pad4) -> Net-(Q102-Pad3)
- R118 pad 2: Net-(Q103-Pad4) -> Net-(Q103-Pad3)
- R120 pad 2: Net-(Q107-Pad4) -> Net-(Q107-Pad3)
- R122 pad 2: Net-(Q108-Pad4) -> Net-(Q108-Pad3)
- R124 pad 2: Net-(Q109-Pad4) -> Net-(Q109-Pad3)
- R126 pad 2: Net-(Q110-Pad4) -> Net-(Q110-Pad3)
- R128 pad 2: Net-(Q111-Pad4) -> Net-(Q111-Pad3)
- R13 pad 2: Net-(Q15-Pad4) -> Net-(Q15-Pad3)
- R130 pad 2: Net-(Q112-Pad4) -> Net-(Q112-Pad3)
- R132 pad 2: Net-(Q116-Pad4) -> Net-(Q116-Pad3)
- R134 pad 2: Net-(Q117-Pad4) -> Net-(Q117-Pad3)
- R136 pad 2: Net-(Q118-Pad4) -> Net-(Q118-Pad3)
- R138 pad 2: Net-(Q120-Pad4) -> Net-(Q120-Pad3)
- R140 pad 2: Net-(Q122-Pad4) -> Net-(Q122-Pad3)
- R142 pad 2: Net-(Q124-Pad4) -> Net-(Q124-Pad3)
- R144 pad 2: Net-(Q128-Pad4) -> Net-(Q128-Pad3)
- R146 pad 2: Net-(Q129-Pad4) -> Net-(Q129-Pad3)
- R148 pad 2: Net-(Q130-Pad4) -> Net-(Q130-Pad3)
- R15 pad 2: Net-(Q13-Pad4) -> Net-(Q13-Pad3)
- R150 pad 2: Net-(Q131-Pad4) -> Net-(Q131-Pad3)
- R152 pad 2: Net-(Q132-Pad4) -> Net-(Q132-Pad3)
- R154 pad 2: Net-(Q133-Pad4) -> Net-(Q133-Pad3)
- R156 pad 2: Net-(Q137-Pad4) -> Net-(Q137-Pad3)
- R158 pad 2: Net-(Q138-Pad4) -> Net-(Q138-Pad3)
- R160 pad 2: Net-(Q139-Pad4) -> Net-(Q139-Pad3)
- R162 pad 2: Net-(Q140-Pad4) -> Net-(Q140-Pad3)
- R164 pad 2: Net-(Q141-Pad4) -> Net-(Q141-Pad3)
- R166 pad 2: Net-(Q142-Pad4) -> Net-(Q142-Pad3)
- R168 pad 2: Net-(Q146-Pad4) -> Net-(Q146-Pad3)
- R17 pad 2: Net-(Q14-Pad4) -> Net-(Q14-Pad3)
- R170 pad 2: Net-(Q147-Pad4) -> Net-(Q147-Pad3)
- R172 pad 2: Net-(Q148-Pad4) -> Net-(Q148-Pad3)
- R174 pad 2: Net-(Q152-Pad4) -> Net-(Q152-Pad3)
- R176 pad 2: Net-(Q153-Pad4) -> Net-(Q153-Pad3)
- R178 pad 2: Net-(Q154-Pad4) -> Net-(Q154-Pad3)
- R180 pad 2: Net-(Q156-Pad4) -> Net-(Q156-Pad3)
- R182 pad 2: Net-(Q158-Pad4) -> Net-(Q158-Pad3)
- R184 pad 2: Net-(Q160-Pad4) -> Net-(Q160-Pad3)
- R186 pad 2: Net-(Q164-Pad4) -> Net-(Q164-Pad3)
- R188 pad 2: Net-(Q165-Pad4) -> Net-(Q165-Pad3)
- R190 pad 2: Net-(Q166-Pad4) -> Net-(Q166-Pad3)
- R192 pad 2: Net-(Q167-Pad4) -> Net-(Q167-Pad3)
- R194 pad 2: Net-(Q168-Pad4) -> Net-(Q168-Pad3)
- R196 pad 2: Net-(Q169-Pad4) -> Net-(Q169-Pad3)
- R198 pad 2: Net-(Q173-Pad4) -> Net-(Q173-Pad3)
- R2 pad 2: Net-(Q1-Pad3) -> Net-(Q1-Pad4)
- R20 pad 2: Net-(Q19-Pad4) -> Net-(Q19-Pad3)
- R200 pad 2: Net-(Q174-Pad4) -> Net-(Q174-Pad3)
- R202 pad 2: Net-(Q175-Pad4) -> Net-(Q175-Pad3)
- R204 pad 2: Net-(Q176-Pad4) -> Net-(Q176-Pad3)
- R206 pad 2: Net-(Q177-Pad4) -> Net-(Q177-Pad3)
- R208 pad 2: Net-(Q178-Pad4) -> Net-(Q178-Pad3)
- R210 pad 2: Net-(Q182-Pad4) -> Net-(Q182-Pad3)
- R212 pad 2: Net-(Q183-Pad4) -> Net-(Q183-Pad3)
- R214 pad 2: Net-(Q184-Pad4) -> Net-(Q184-Pad3)
- R216 pad 2: Net-(Q186-Pad4) -> Net-(Q186-Pad3)
- R218 pad 2: Net-(Q188-Pad4) -> Net-(Q188-Pad3)
- R22 pad 2: Net-(Q21-Pad4) -> Net-(Q21-Pad3)
- R220 pad 2: Net-(Q190-Pad4) -> Net-(Q190-Pad3)
- R222 pad 2: Net-(Q194-Pad4) -> Net-(Q194-Pad3)
- R224 pad 2: Net-(Q195-Pad4) -> Net-(Q195-Pad3)
- R226 pad 2: Net-(Q196-Pad4) -> Net-(Q196-Pad3)
- R228 pad 2: Net-(Q197-Pad4) -> Net-(Q197-Pad3)
- R230 pad 2: Net-(Q198-Pad4) -> Net-(Q198-Pad3)
- R232 pad 2: Net-(Q199-Pad4) -> Net-(Q199-Pad3)
- R234 pad 2: Net-(Q203-Pad4) -> Net-(Q203-Pad3)
- R236 pad 2: Net-(Q204-Pad4) -> Net-(Q204-Pad3)
- R238 pad 2: Net-(Q205-Pad4) -> Net-(Q205-Pad3)
- R24 pad 2: Net-(Q24-Pad4) -> Net-(Q24-Pad3)
- R240 pad 2: Net-(Q206-Pad4) -> Net-(Q206-Pad3)
- R242 pad 2: Net-(Q207-Pad4) -> Net-(Q207-Pad3)
- R244 pad 2: Net-(Q208-Pad4) -> Net-(Q208-Pad3)
- R246 pad 2: Net-(Q212-Pad4) -> Net-(Q212-Pad3)
- R248 pad 2: Net-(Q213-Pad4) -> Net-(Q213-Pad3)
- R250 pad 2: Net-(Q214-Pad4) -> Net-(Q214-Pad3)
- R252 pad 2: Net-(Q218-Pad4) -> Net-(Q218-Pad3)
- R254 pad 2: Net-(Q219-Pad4) -> Net-(Q219-Pad3)
- R256 pad 2: Net-(Q220-Pad4) -> Net-(Q220-Pad3)
- R26 pad 2: Net-(Q26-Pad4) -> Net-(Q26-Pad3)
- R28 pad 2: Net-(Q28-Pad4) -> Net-(Q28-Pad3)
- R3 pad 2: Net-(Q4-Pad4) -> Net-(Q4-Pad3)
- R30 pad 2: Net-(Q32-Pad4) -> Net-(Q32-Pad3)
- R32 pad 2: Net-(Q33-Pad4) -> Net-(Q33-Pad3)
- R34 pad 2: Net-(Q34-Pad4) -> Net-(Q34-Pad3)
- R36 pad 2: Net-(Q35-Pad4) -> Net-(Q35-Pad3)
- R38 pad 2: Net-(Q36-Pad4) -> Net-(Q36-Pad3)
- R40 pad 2: Net-(Q37-Pad4) -> Net-(Q37-Pad3)
- R42 pad 2: Net-(Q41-Pad4) -> Net-(Q41-Pad3)
- R44 pad 2: Net-(Q42-Pad4) -> Net-(Q42-Pad3)
- R46 pad 2: Net-(Q43-Pad4) -> Net-(Q43-Pad3)
- R48 pad 2: Net-(Q44-Pad4) -> Net-(Q44-Pad3)
- R5 pad 2: Net-(Q2-Pad4) -> Net-(Q2-Pad3)
- R50 pad 2: Net-(Q45-Pad4) -> Net-(Q45-Pad3)
- R52 pad 2: Net-(Q46-Pad4) -> Net-(Q46-Pad3)
- R54 pad 2: Net-(Q50-Pad4) -> Net-(Q50-Pad3)
- R56 pad 2: Net-(Q51-Pad4) -> Net-(Q51-Pad3)
- R58 pad 2: Net-(Q52-Pad4) -> Net-(Q52-Pad3)
- R60 pad 2: Net-(Q54-Pad4) -> Net-(Q54-Pad3)
- R62 pad 2: Net-(Q56-Pad4) -> Net-(Q56-Pad3)
- R64 pad 2: Net-(Q58-Pad4) -> Net-(Q58-Pad3)
- R66 pad 2: Net-(Q62-Pad4) -> Net-(Q62-Pad3)
- R68 pad 2: Net-(Q63-Pad4) -> Net-(Q63-Pad3)
- R7 pad 2: Net-(Q3-Pad4) -> Net-(Q3-Pad3)
- R70 pad 2: Net-(Q64-Pad4) -> Net-(Q64-Pad3)
- R72 pad 2: Net-(Q65-Pad4) -> Net-(Q65-Pad3)
- R74 pad 2: Net-(Q66-Pad4) -> Net-(Q66-Pad3)
- R76 pad 2: Net-(Q67-Pad4) -> Net-(Q67-Pad3)
- R78 pad 2: Net-(Q71-Pad4) -> Net-(Q71-Pad3)
- R80 pad 2: Net-(Q72-Pad4) -> Net-(Q72-Pad3)
- R82 pad 2: Net-(Q73-Pad4) -> Net-(Q73-Pad3)
- R84 pad 2: Net-(Q74-Pad4) -> Net-(Q74-Pad3)
- R86 pad 2: Net-(Q75-Pad4) -> Net-(Q75-Pad3)
- R88 pad 2: Net-(Q76-Pad4) -> Net-(Q76-Pad3)
- R9 pad 2: Net-(Q10-Pad4) -> Net-(Q10-Pad3)
- R90 pad 2: Net-(Q80-Pad4) -> Net-(Q80-Pad3)
- R92 pad 2: Net-(Q81-Pad4) -> Net-(Q81-Pad3)
- R94 pad 2: Net-(Q82-Pad4) -> Net-(Q82-Pad3)
- R96 pad 2: Net-(Q86-Pad4) -> Net-(Q86-Pad3)
- R98 pad 2: Net-(Q87-Pad4) -> Net-(Q87-Pad3)
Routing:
- net /adder/Vdd: track 0.00 -> 147.5 mm, vias 0 -> 137
- net /adder/Vss: track 0.00 -> 142.7 mm, vias 0 -> 137
- net GND: track 0.00 -> 87.4 mm, vias 0 -> 4
- net Net-(Q95-Pad2): track 0.00 -> 76.3 mm, vias 0 -> 3
- net Net-(Q96-Pad2): track 0.00 -> 76.3 mm, vias 0 -> 3
- net Net-(Q163-Pad2): track 0.00 -> 76.3 mm, vias 0 -> 3
- net Net-(Q162-Pad2): track 0.00 -> 76.3 mm, vias 0 -> 3
- net Net-(Q161-Pad2): track 0.00 -> 76.3 mm, vias 0 -> 3
- net Net-(Q100-Pad2): track 0.00 -> 76.3 mm, vias 0 -> 3
- net Net-(Q31-Pad2): track 0.00 -> 76.3 mm, vias 0 -> 3
- net Net-(Q30-Pad2): track 0.00 -> 76.3 mm, vias 0 -> 3
- net Net-(Q1-Pad2): track 0.00 -> 65.5 mm, vias 0 -> 2
- net OutputEnable: track 0.00 -> 65.4 mm, vias 0 -> 2
- net Net-(Q37-Pad2): track 0.00 -> 64.8 mm, vias 0 -> 2
- net Net-(Q36-Pad2): track 0.00 -> 64.8 mm, vias 0 -> 2
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- added copper zone on In1.Cu, net /adder/Vdd
- added copper zone on In2.Cu, net /adder/Vss
- added copper zone on In1.Cu, net Vdd
- added copper zone on In2.Cu, net Vss
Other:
- copper layers 2 -> 4
- board text added: "9-trit ternary adder circuit rev.1"
- board text added: "A0"
- board text added: "A1"
- board text added: "A2"
- board text added: "A3"
- board text added: "A4"
- board text added: "A5"
- board text added: "A6"
- board text added: "A7"
- board text added: "A8"
- board text added: "B0"
- board text added: "B1"
- board text added: "B2"
- board text added: "B3"
- board text added: "B4"
- board text added: "B5"
- board text added: "B6"
- board text added: "B7"
- board text added: "B8"
- board text added: "CarryIn"
- board text added: "CarryOut"
- board text added: "FnA0"
- board text added: "FnB0"
- board text added: "FnB1"
- board text added: "GND"
- board text added: "OutputEnable"
- board text added: "R0"
- board text added: "R1"
- board text added: "R2"
- board text added: "R3"
- board text added: "R4"
- board text added: "R5"
- board text added: "R6"
- board text added: "R7"
- board text added: "R8"
- board text added: "Vdd"
- board text added: "Vss"
